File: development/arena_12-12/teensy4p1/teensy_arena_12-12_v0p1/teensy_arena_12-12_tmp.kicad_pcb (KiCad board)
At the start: 4 copper layers, 228.6 x 228.6 mm, 51 parts, among them J1 Barrel_Jack, J2 Conn_01x04, J3 Conn_01x04, P1 CONN15, P10 CONN15, P11 CONN15, P12 CONN15, P2 CONN15, P3 CONN15, P4 CONN15, P5 CONN15, P6 CONN15, P7 CONN15, P8 CONN15, P9 CONN15, Q2 MOSFET_NCHAN, SW1 SW_SPDT, U1 TXB0108PW, U18 Teensy4.1, U2 TXB0108PW, U3 TXB0108PW, U4 TXB0108PW, U5 TXB0108PW

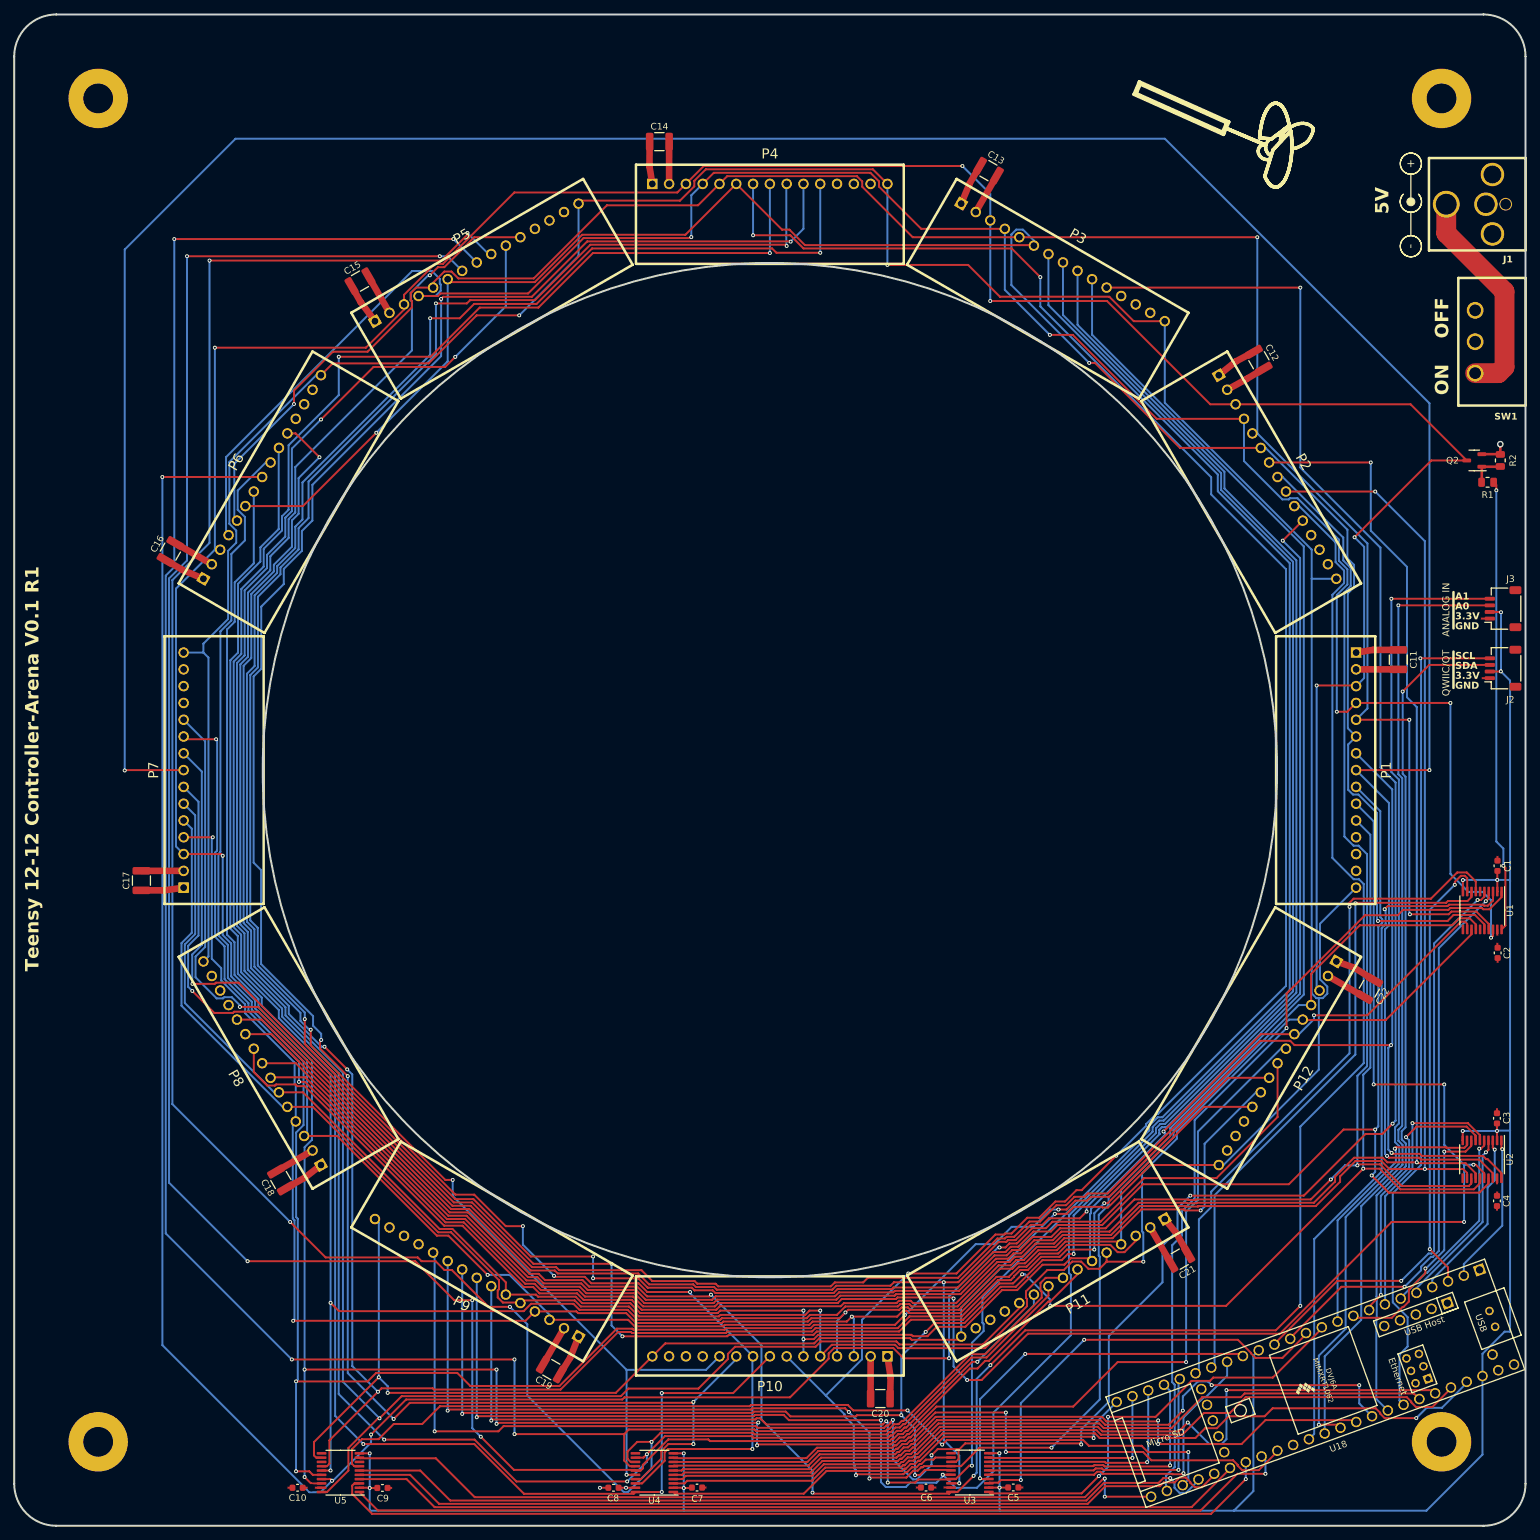
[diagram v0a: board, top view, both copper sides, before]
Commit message: Finished hand route of 12-12 teensy arena. Finished route of 12-12 top.
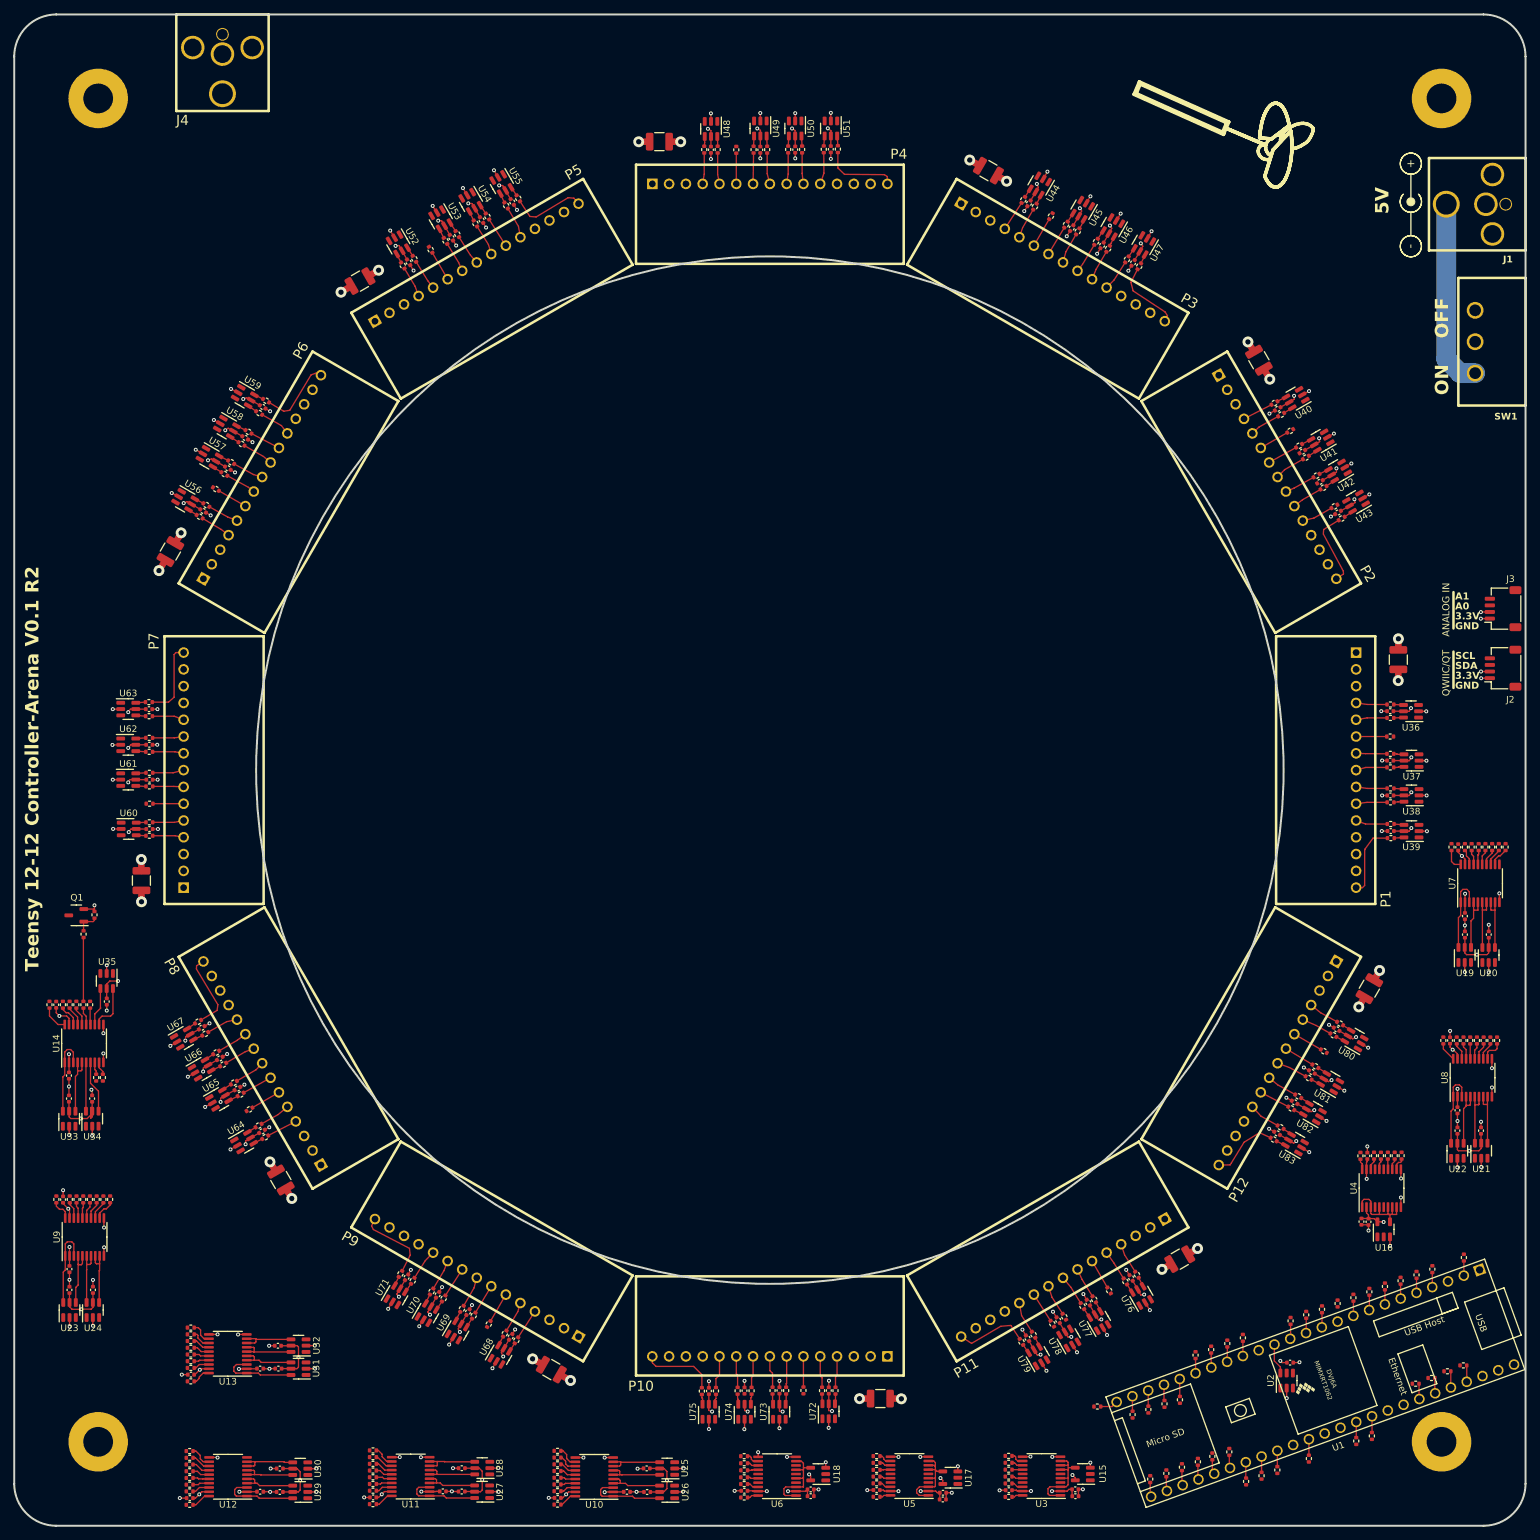
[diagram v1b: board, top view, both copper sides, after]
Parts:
- removed Q2: MOSFET_NCHAN, Package_TO_SOT_SMD:SOT-23-3
- removed the U1 at (285.6, 199.0)
- added C11: 0.1uF, Capacitor_SMD:C_0402_1005Metric, F.Cu at (281.9, 189.5)
- added C12: 0.1uF, Capacitor_SMD:C_0402_1005Metric, F.Cu at (281.8, 229.3)
- added C13: 0.1uF, Capacitor_SMD:C_0402_1005Metric, F.Cu at (280.7, 218.7)
- added C14: 0.1uF, Capacitor_SMD:C_0402_1005Metric, F.Cu at (71.9, 253.3)
- added C15: 0.1uF, Capacitor_SMD:C_0402_1005Metric, F.Cu at (70.9, 242.8)
- added C16: 0.1uF, Capacitor_SMD:C_0402_1005Metric, F.Cu at (156.2, 287.0)
- added C17: 0.1uF, Capacitor_SMD:C_0402_1005Metric, F.Cu at (145.7, 287.9)
- added C18: 0.1uF, Capacitor_SMD:C_0402_1005Metric, F.Cu at (128.3, 286.9)
- added C19: 0.1uF, Capacitor_SMD:C_0402_1005Metric, F.Cu at (117.8, 287.8)
- added C20: 0.1uF, Capacitor_SMD:C_0402_1005Metric, F.Cu at (100.7, 287.0)
- added C21: 0.1uF, Capacitor_SMD:C_0402_1005Metric, F.Cu at (90.1, 287.9)
- added C22: 0.1uF, Capacitor_SMD:C_0402_1005Metric, F.Cu at (100.7, 268.3)
- added C23: 0.1uF, Capacitor_SMD:C_0402_1005Metric, F.Cu at (90.2, 269.2)
- added C24: 0.1uF, Capacitor_SMD:C_0402_1005Metric, F.Cu at (71.8, 224.0)
- added C25: 0.1uF, Capacitor_SMD:C_0402_1005Metric, F.Cu at (69.8, 213.3)
- added C26: 0.1uF, Capacitor_SMD:C_0402_1005Metric, F.Cu at (224.0, 286.6)
- added C27: 0.1uF, Capacitor_SMD:C_0402_1005Metric, F.Cu at (268.4, 246.1)
- added C28: 0.1uF, Capacitor_SMD:C_0402_1005Metric, F.Cu at (204.0, 287.1)
- added C29: 0.1uF, Capacitor_SMD:C_0402_1005Metric, F.Cu at (184.0, 286.6)
- added C30: 0.1uF, Capacitor_SMD:C_0402_1005Metric, F.Cu at (282.9, 202.7)
- added C31: 0.1uF, Capacitor_SMD:C_0402_1005Metric, F.Cu at (286.5, 202.7)
- added C32: 0.1uF, Capacitor_SMD:C_0402_1005Metric, F.Cu at (281.8, 232.3)
- added C33: 0.1uF, Capacitor_SMD:C_0402_1005Metric, F.Cu at (285.4, 232.3)
- added C34: 0.1uF, Capacitor_SMD:C_0402_1005Metric, F.Cu at (71.9, 256.4)
- added C35: 0.1uF, Capacitor_SMD:C_0402_1005Metric, F.Cu at (75.4, 256.4)
- added C36: 0.1uF, Capacitor_SMD:C_0402_1005Metric, F.Cu at (159.2, 283.4)
- added C37: 0.1uF, Capacitor_SMD:C_0402_1005Metric, F.Cu at (159.2, 287.0)
- added C38: 0.1uF, Capacitor_SMD:C_0402_1005Metric, F.Cu at (131.2, 286.9)
- added C39: 0.1uF, Capacitor_SMD:C_0402_1005Metric, F.Cu at (131.2, 283.4)
- added C40: 0.1uF, Capacitor_SMD:C_0402_1005Metric, F.Cu at (103.7, 287.0)
- added C41: 0.1uF, Capacitor_SMD:C_0402_1005Metric, F.Cu at (103.7, 283.4)
- added C42: 0.1uF, Capacitor_SMD:C_0402_1005Metric, F.Cu at (103.5, 268.3)
- added C43: 0.1uF, Capacitor_SMD:C_0402_1005Metric, F.Cu at (103.4, 264.9)
- added C44: 0.1uF, Capacitor_SMD:C_0402_1005Metric, F.Cu at (71.8, 227.5)
- added C45: 0.1uF, Capacitor_SMD:C_0402_1005Metric, F.Cu at (75.3, 227.5)
- added C46: 0.1uF, Capacitor_SMD:C_0402_1005Metric, F.Cu at (77.5, 212.8)
- added C47: 0.1uF, Capacitor_SMD:C_0402_1005Metric, F.Cu at (271.6, 168.9)
- added C48: 0.1uF, Capacitor_SMD:C_0402_1005Metric, F.Cu at (271.6, 176.4)
- added C49: 0.1uF, Capacitor_SMD:C_0402_1005Metric, F.Cu at (271.7, 181.6)
- added C50: 0.1uF, Capacitor_SMD:C_0402_1005Metric, F.Cu at (271.7, 187.0)
- added C51: 0.1uF, Capacitor_SMD:C_0402_1005Metric, F.Cu at (254.6, 123.2)
- added C52: 0.1uF, Capacitor_SMD:C_0402_1005Metric, F.Cu at (258.3, 129.6)
- added C53: 0.1uF, Capacitor_SMD:C_0402_1005Metric, F.Cu at (261.0, 134.2)
- added C54: 0.1uF, Capacitor_SMD:C_0402_1005Metric, F.Cu at (263.7, 138.8)
- added C55: 0.1uF, Capacitor_SMD:C_0402_1005Metric, F.Cu at (217.0, 92.1)
- added C56: 0.1uF, Capacitor_SMD:C_0402_1005Metric, F.Cu at (223.5, 95.8)
- added C57: 0.1uF, Capacitor_SMD:C_0402_1005Metric, F.Cu at (228.1, 98.4)
- added C58: 0.1uF, Capacitor_SMD:C_0402_1005Metric, F.Cu at (232.7, 101.1)
- added C59: 0.1uF, Capacitor_SMD:C_0402_1005Metric, F.Cu at (168.9, 84.0)
- added C60: 0.1uF, Capacitor_SMD:C_0402_1005Metric, F.Cu at (176.4, 84.0)
- added C61: 0.1uF, Capacitor_SMD:C_0402_1005Metric, F.Cu at (181.6, 83.9)
- added C62: 0.1uF, Capacitor_SMD:C_0402_1005Metric, F.Cu at (187.0, 83.9)
- added C63: 0.1uF, Capacitor_SMD:C_0402_1005Metric, F.Cu at (123.2, 101.0)
- added C64: 0.1uF, Capacitor_SMD:C_0402_1005Metric, F.Cu at (129.6, 97.3)
- added C65: 0.1uF, Capacitor_SMD:C_0402_1005Metric, F.Cu at (134.2, 94.6)
- added C66: 0.1uF, Capacitor_SMD:C_0402_1005Metric, F.Cu at (138.8, 91.9)
- added C67: 0.1uF, Capacitor_SMD:C_0402_1005Metric, F.Cu at (92.1, 138.6)
- added C68: 0.1uF, Capacitor_SMD:C_0402_1005Metric, F.Cu at (95.8, 132.1)
- added C69: 0.1uF, Capacitor_SMD:C_0402_1005Metric, F.Cu at (98.4, 127.5)
- added C70: 0.1uF, Capacitor_SMD:C_0402_1005Metric, F.Cu at (101.1, 122.9)
- added C71: 0.1uF, Capacitor_SMD:C_0402_1005Metric, F.Cu at (84.0, 186.7)
- added C72: 0.1uF, Capacitor_SMD:C_0402_1005Metric, F.Cu at (84.0, 179.2)
- added C73: 0.1uF, Capacitor_SMD:C_0402_1005Metric, F.Cu at (83.9, 174.0)
- added C74: 0.1uF, Capacitor_SMD:C_0402_1005Metric, F.Cu at (83.9, 168.6)
- added C75: 0.1uF, Capacitor_SMD:C_0402_1005Metric, F.Cu at (101.0, 232.4)
- added C76: 0.1uF, Capacitor_SMD:C_0402_1005Metric, F.Cu at (97.3, 226.0)
- added C77: 0.1uF, Capacitor_SMD:C_0402_1005Metric, F.Cu at (94.6, 221.4)
- added C78: 0.1uF, Capacitor_SMD:C_0402_1005Metric, F.Cu at (91.9, 216.8)
- added C79: 0.1uF, Capacitor_SMD:C_0402_1005Metric, F.Cu at (138.6, 263.5)
- added C80: 0.1uF, Capacitor_SMD:C_0402_1005Metric, F.Cu at (132.1, 259.8)
- added C81: 0.1uF, Capacitor_SMD:C_0402_1005Metric, F.Cu at (127.5, 257.2)
- added C82: 0.1uF, Capacitor_SMD:C_0402_1005Metric, F.Cu at (122.9, 254.5)
- added C83: 0.1uF, Capacitor_SMD:C_0402_1005Metric, F.Cu at (186.7, 271.6)
- added C84: 0.1uF, Capacitor_SMD:C_0402_1005Metric, F.Cu at (179.2, 271.6)
- added C85: 0.1uF, Capacitor_SMD:C_0402_1005Metric, F.Cu at (174.0, 271.7)
- added C86: 0.1uF, Capacitor_SMD:C_0402_1005Metric, F.Cu at (168.6, 271.7)
- added C87: 0.1uF, Capacitor_SMD:C_0402_1005Metric, F.Cu at (232.4, 254.6)
- added C88: 0.1uF, Capacitor_SMD:C_0402_1005Metric, F.Cu at (226.0, 258.3)
- added C89: 0.1uF, Capacitor_SMD:C_0402_1005Metric, F.Cu at (221.4, 261.0)
- added C90: 0.1uF, Capacitor_SMD:C_0402_1005Metric, F.Cu at (216.8, 263.7)
- added C91: 0.1uF, Capacitor_SMD:C_0402_1005Metric, F.Cu at (263.5, 217.0)
- added C92: 0.1uF, Capacitor_SMD:C_0402_1005Metric, F.Cu at (259.8, 223.5)
- added C93: 0.1uF, Capacitor_SMD:C_0402_1005Metric, F.Cu at (257.2, 228.1)
- added C94: 0.1uF, Capacitor_SMD:C_0402_1005Metric, F.Cu at (254.5, 232.7)
- added J4: Barrel_Jack, arena_custom:DCJACK_2PIN_HIGHCURRENT, F.Cu at (95.0, 63.5)
- added Q1: MOSFET_NCHAN, Package_TO_SOT_SMD:SOT-23-3, F.Cu at (72.9, 199.8)
- added R10: 68, Resistor_SMD:R_0402_1005Metric, F.Cu at (275.6, 254.2)
- added R100: 68, Resistor_SMD:R_0402_1005Metric, F.Cu at (117.8, 282.7)
- added R101: 68, Resistor_SMD:R_0402_1005Metric, F.Cu at (117.8, 281.7)
- added R102: 68, Resistor_SMD:R_0402_1005Metric, F.Cu at (117.8, 280.7)
- added R103: 68, Resistor_SMD:R_0402_1005Metric, F.Cu at (90.0, 288.9)
- added R104: 68, Resistor_SMD:R_0402_1005Metric, F.Cu at (90.0, 286.9)
- added R105: 68, Resistor_SMD:R_0402_1005Metric, F.Cu at (90.0, 285.9)
- added R106: 68, Resistor_SMD:R_0402_1005Metric, F.Cu at (90.0, 284.9)
- added R107: 68, Resistor_SMD:R_0402_1005Metric, F.Cu at (90.0, 283.9)
- added R108: 68, Resistor_SMD:R_0402_1005Metric, F.Cu at (90.0, 282.8)
- added R109: 68, Resistor_SMD:R_0402_1005Metric, F.Cu at (90.0, 281.8)
- added R11: 68, Resistor_SMD:R_0402_1005Metric, F.Cu at (273.2, 255.0)
- added R110: 68, Resistor_SMD:R_0402_1005Metric, F.Cu at (90.0, 280.8)
- added R111: 68, Resistor_SMD:R_0402_1005Metric, F.Cu at (90.2, 270.3)
- added R112: 68, Resistor_SMD:R_0402_1005Metric, F.Cu at (90.2, 268.2)
- added R113: 68, Resistor_SMD:R_0402_1005Metric, F.Cu at (90.2, 267.2)
- added R114: 68, Resistor_SMD:R_0402_1005Metric, F.Cu at (90.2, 266.2)
- added R115: 68, Resistor_SMD:R_0402_1005Metric, F.Cu at (90.2, 265.2)
- added R116: 68, Resistor_SMD:R_0402_1005Metric, F.Cu at (90.2, 264.2)
- added R117: 68, Resistor_SMD:R_0402_1005Metric, F.Cu at (90.2, 263.1)
- added R118: 68, Resistor_SMD:R_0402_1005Metric, F.Cu at (90.2, 262.1)
- added R119: 68, Resistor_SMD:R_0402_1005Metric, F.Cu at (68.8, 213.3)
- added R12: 68, Resistor_SMD:R_0402_1005Metric, F.Cu at (270.8, 255.9)
- added R120: 68, Resistor_SMD:R_0402_1005Metric, F.Cu at (70.9, 213.3)
- added R121: 68, Resistor_SMD:R_0402_1005Metric, F.Cu at (71.9, 213.3)
- added R122: 68, Resistor_SMD:R_0402_1005Metric, F.Cu at (72.9, 213.3)
- added R123: 68, Resistor_SMD:R_0402_1005Metric, F.Cu at (74.0, 213.3)
- added R124: 68, Resistor_SMD:R_0402_1005Metric, F.Cu at (75.0, 213.3)
- added R125: 68, Resistor_SMD:R_0402_1005Metric, F.Cu at (75.9, 224.3)
- added R126: 68, Resistor_SMD:R_0402_1005Metric, F.Cu at (76.9, 224.3)
- added R127: 68, Resistor_SMD:R_0402_1005Metric, F.Cu at (271.7, 167.9)
- added R128: 68, Resistor_SMD:R_0402_1005Metric, F.Cu at (271.7, 169.9)
- added R129: 68, Resistor_SMD:R_0402_1005Metric, F.Cu at (271.7, 175.3)
- added R13: 68, Resistor_SMD:R_0402_1005Metric, F.Cu at (268.5, 256.7)
- added R130: 68, Resistor_SMD:R_0402_1005Metric, F.Cu at (271.7, 177.4)
- added R131: 68, Resistor_SMD:R_0402_1005Metric, F.Cu at (271.7, 180.6)
- added R132: 68, Resistor_SMD:R_0402_1005Metric, F.Cu at (271.7, 182.7)
- added R133: 68, Resistor_SMD:R_0402_1005Metric, F.Cu at (271.7, 186.0)
- added R134: 68, Resistor_SMD:R_0402_1005Metric, F.Cu at (271.7, 188.1)
- added R135: 68, Resistor_SMD:R_0402_1005Metric, F.Cu at (254.1, 122.3)
- added R136: 68, Resistor_SMD:R_0402_1005Metric, F.Cu at (255.1, 124.0)
- added R137: 68, Resistor_SMD:R_0402_1005Metric, F.Cu at (257.8, 128.7)
- added R138: 68, Resistor_SMD:R_0402_1005Metric, F.Cu at (258.9, 130.5)
- added R139: 68, Resistor_SMD:R_0402_1005Metric, F.Cu at (260.5, 133.3)
- added R14: 68, Resistor_SMD:R_0402_1005Metric, F.Cu at (266.1, 257.6)
- added R140: 68, Resistor_SMD:R_0402_1005Metric, F.Cu at (261.5, 135.1)
- added R141: 68, Resistor_SMD:R_0402_1005Metric, F.Cu at (263.2, 137.9)
- added R142: 68, Resistor_SMD:R_0402_1005Metric, F.Cu at (264.3, 139.7)
- added R143: 68, Resistor_SMD:R_0402_1005Metric, F.Cu at (216.1, 91.5)
- added R144: 68, Resistor_SMD:R_0402_1005Metric, F.Cu at (217.9, 92.6)
- added R145: 68, Resistor_SMD:R_0402_1005Metric, F.Cu at (222.6, 95.3)
- added R146: 68, Resistor_SMD:R_0402_1005Metric, F.Cu at (224.4, 96.3)
- added R147: 68, Resistor_SMD:R_0402_1005Metric, F.Cu at (227.1, 97.9)
- added R148: 68, Resistor_SMD:R_0402_1005Metric, F.Cu at (229.0, 98.9)
- added R149: 68, Resistor_SMD:R_0402_1005Metric, F.Cu at (231.8, 100.6)
- added R15: 68, Resistor_SMD:R_0402_1005Metric, F.Cu at (263.7, 258.5)
- added R150: 68, Resistor_SMD:R_0402_1005Metric, F.Cu at (233.7, 101.6)
- added R151: 68, Resistor_SMD:R_0402_1005Metric, F.Cu at (167.9, 83.9)
- added R152: 68, Resistor_SMD:R_0402_1005Metric, F.Cu at (169.9, 83.9)
- added R153: 68, Resistor_SMD:R_0402_1005Metric, F.Cu at (175.3, 83.9)
- added R154: 68, Resistor_SMD:R_0402_1005Metric, F.Cu at (177.4, 83.9)
- added R155: 68, Resistor_SMD:R_0402_1005Metric, F.Cu at (180.6, 83.9)
- added R156: 68, Resistor_SMD:R_0402_1005Metric, F.Cu at (182.7, 83.9)
- added R157: 68, Resistor_SMD:R_0402_1005Metric, F.Cu at (186.0, 83.9)
- added R158: 68, Resistor_SMD:R_0402_1005Metric, F.Cu at (188.1, 83.9)
- added R159: 68, Resistor_SMD:R_0402_1005Metric, F.Cu at (122.3, 101.5)
- added R16: 68, Resistor_SMD:R_0402_1005Metric, F.Cu at (261.3, 259.4)
- added R160: 68, Resistor_SMD:R_0402_1005Metric, F.Cu at (124.0, 100.5)
- added R161: 68, Resistor_SMD:R_0402_1005Metric, F.Cu at (128.7, 97.8)
- added R162: 68, Resistor_SMD:R_0402_1005Metric, F.Cu at (130.5, 96.7)
- added R163: 68, Resistor_SMD:R_0402_1005Metric, F.Cu at (133.3, 95.1)
- added R164: 68, Resistor_SMD:R_0402_1005Metric, F.Cu at (135.1, 94.1)
- added R165: 68, Resistor_SMD:R_0402_1005Metric, F.Cu at (137.9, 92.4)
- added R166: 68, Resistor_SMD:R_0402_1005Metric, F.Cu at (139.7, 91.3)
- added R167: 68, Resistor_SMD:R_0402_1005Metric, F.Cu at (91.5, 139.5)
- added R168: 68, Resistor_SMD:R_0402_1005Metric, F.Cu at (92.6, 137.7)
- added R169: 68, Resistor_SMD:R_0402_1005Metric, F.Cu at (95.3, 133.0)
- added R17: 68, Resistor_SMD:R_0402_1005Metric, F.Cu at (258.9, 260.2)
- added R170: 68, Resistor_SMD:R_0402_1005Metric, F.Cu at (96.3, 131.2)
- added R171: 68, Resistor_SMD:R_0402_1005Metric, F.Cu at (97.9, 128.5)
- added R172: 68, Resistor_SMD:R_0402_1005Metric, F.Cu at (98.9, 126.6)
- added R173: 68, Resistor_SMD:R_0402_1005Metric, F.Cu at (100.6, 123.8)
- added R174: 68, Resistor_SMD:R_0402_1005Metric, F.Cu at (101.6, 121.9)
- added R175: 68, Resistor_SMD:R_0402_1005Metric, F.Cu at (83.9, 187.7)
- added R176: 68, Resistor_SMD:R_0402_1005Metric, F.Cu at (83.9, 185.7)
- added R177: 68, Resistor_SMD:R_0402_1005Metric, F.Cu at (83.9, 180.3)
- added R178: 68, Resistor_SMD:R_0402_1005Metric, F.Cu at (83.9, 178.2)
- added R179: 68, Resistor_SMD:R_0402_1005Metric, F.Cu at (83.9, 175.0)
- added R18: 68, Resistor_SMD:R_0402_1005Metric, F.Cu at (249.4, 263.7)
- added R180: 68, Resistor_SMD:R_0402_1005Metric, F.Cu at (83.9, 172.9)
- added R181: 68, Resistor_SMD:R_0402_1005Metric, F.Cu at (83.9, 169.6)
- added R182: 68, Resistor_SMD:R_0402_1005Metric, F.Cu at (83.9, 167.5)
- added R183: 68, Resistor_SMD:R_0402_1005Metric, F.Cu at (101.5, 233.3)
- added R184: 68, Resistor_SMD:R_0402_1005Metric, F.Cu at (100.5, 231.6)
- added R185: 68, Resistor_SMD:R_0402_1005Metric, F.Cu at (97.8, 226.9)
- added R186: 68, Resistor_SMD:R_0402_1005Metric, F.Cu at (96.7, 225.1)
- added R187: 68, Resistor_SMD:R_0402_1005Metric, F.Cu at (95.1, 222.3)
- added R188: 68, Resistor_SMD:R_0402_1005Metric, F.Cu at (94.1, 220.5)
- added R189: 68, Resistor_SMD:R_0402_1005Metric, F.Cu at (92.4, 217.7)
- added R19: 68, Resistor_SMD:R_0402_1005Metric, F.Cu at (247.0, 264.5)
- added R190: 68, Resistor_SMD:R_0402_1005Metric, F.Cu at (91.3, 215.9)
- added R191: 68, Resistor_SMD:R_0402_1005Metric, F.Cu at (139.5, 264.1)
- added R192: 68, Resistor_SMD:R_0402_1005Metric, F.Cu at (137.7, 263.0)
- added R193: 68, Resistor_SMD:R_0402_1005Metric, F.Cu at (133.0, 260.3)
- added R194: 68, Resistor_SMD:R_0402_1005Metric, F.Cu at (131.2, 259.3)
- added R195: 68, Resistor_SMD:R_0402_1005Metric, F.Cu at (128.5, 257.7)
- added R196: 68, Resistor_SMD:R_0402_1005Metric, F.Cu at (126.6, 256.7)
- added R197: 68, Resistor_SMD:R_0402_1005Metric, F.Cu at (123.8, 255.0)
- added R198: 68, Resistor_SMD:R_0402_1005Metric, F.Cu at (121.9, 254.0)
- added R199: 68, Resistor_SMD:R_0402_1005Metric, F.Cu at (187.7, 271.7)
- added R20: 68, Resistor_SMD:R_0402_1005Metric, F.Cu at (239.8, 273.1)
- added R200: 68, Resistor_SMD:R_0402_1005Metric, F.Cu at (185.7, 271.7)
- added R201: 68, Resistor_SMD:R_0402_1005Metric, F.Cu at (180.3, 271.7)
- added R202: 68, Resistor_SMD:R_0402_1005Metric, F.Cu at (178.2, 271.7)
- added R203: 68, Resistor_SMD:R_0402_1005Metric, F.Cu at (175.0, 271.7)
- added R204: 68, Resistor_SMD:R_0402_1005Metric, F.Cu at (172.9, 271.7)
- added R205: 68, Resistor_SMD:R_0402_1005Metric, F.Cu at (169.6, 271.7)
- added R206: 68, Resistor_SMD:R_0402_1005Metric, F.Cu at (167.5, 271.7)
- added R207: 68, Resistor_SMD:R_0402_1005Metric, F.Cu at (233.3, 254.1)
- added R208: 68, Resistor_SMD:R_0402_1005Metric, F.Cu at (231.6, 255.1)
- added R209: 68, Resistor_SMD:R_0402_1005Metric, F.Cu at (226.9, 257.8)
- added R21: 68, Resistor_SMD:R_0402_1005Metric, F.Cu at (237.5, 273.7)
- added R210: 68, Resistor_SMD:R_0402_1005Metric, F.Cu at (225.1, 258.9)
- added R211: 68, Resistor_SMD:R_0402_1005Metric, F.Cu at (222.3, 260.5)
- added R212: 68, Resistor_SMD:R_0402_1005Metric, F.Cu at (220.5, 261.5)
- added R213: 68, Resistor_SMD:R_0402_1005Metric, F.Cu at (217.7, 263.2)
- added R214: 68, Resistor_SMD:R_0402_1005Metric, F.Cu at (215.9, 264.3)
- added R215: 68, Resistor_SMD:R_0402_1005Metric, F.Cu at (264.1, 216.1)
- added R216: 68, Resistor_SMD:R_0402_1005Metric, F.Cu at (263.0, 217.9)
- added R217: 68, Resistor_SMD:R_0402_1005Metric, F.Cu at (260.3, 222.6)
- added R218: 68, Resistor_SMD:R_0402_1005Metric, F.Cu at (259.3, 224.4)
- added R219: 68, Resistor_SMD:R_0402_1005Metric, F.Cu at (257.7, 227.1)
- added R22: 68, Resistor_SMD:R_0402_1005Metric, F.Cu at (235.1, 274.5)
- added R220: 68, Resistor_SMD:R_0402_1005Metric, F.Cu at (256.7, 229.0)
- added R221: 68, Resistor_SMD:R_0402_1005Metric, F.Cu at (255.0, 231.8)
- added R222: 68, Resistor_SMD:R_0402_1005Metric, F.Cu at (254.0, 233.7)
- added R223: 68, Resistor_SMD:R_0402_1005Metric, F.Cu at (271.6, 172.7)
- added R224: 68, Resistor_SMD:R_0402_1005Metric, F.Cu at (256.5, 126.5)
- added R225: 68, Resistor_SMD:R_0402_1005Metric, F.Cu at (220.3, 94.0)
- added R226: 68, Resistor_SMD:R_0402_1005Metric, F.Cu at (172.7, 84.0)
- added R227: 68, Resistor_SMD:R_0402_1005Metric, F.Cu at (126.5, 99.1)
- added R228: 68, Resistor_SMD:R_0402_1005Metric, F.Cu at (94.0, 135.3)
- added R229: 68, Resistor_SMD:R_0402_1005Metric, F.Cu at (84.0, 182.9)
- added R23: 68, Resistor_SMD:R_0402_1005Metric, F.Cu at (232.7, 275.3)
- added R230: 68, Resistor_SMD:R_0402_1005Metric, F.Cu at (99.1, 229.1)
- added R231: 68, Resistor_SMD:R_0402_1005Metric, F.Cu at (135.3, 261.6)
- added R232: 68, Resistor_SMD:R_0402_1005Metric, F.Cu at (182.9, 271.6)
- added R233: 68, Resistor_SMD:R_0402_1005Metric, F.Cu at (229.1, 256.5)
- added R234: 68, Resistor_SMD:R_0402_1005Metric, F.Cu at (261.6, 220.3)
- added R24: 68, Resistor_SMD:R_0402_1005Metric, F.Cu at (227.3, 274.1)
- added R25: 68, Resistor_SMD:R_0402_1005Metric, F.Cu at (282.7, 267.8)
- added R26: 68, Resistor_SMD:R_0402_1005Metric, F.Cu at (280.3, 268.7)
- added R27: 68, Resistor_SMD:R_0402_1005Metric, F.Cu at (277.9, 269.7)
- added R28: 68, Resistor_SMD:R_0402_1005Metric, F.Cu at (275.5, 270.6)
- added R29: 68, Resistor_SMD:R_0402_1005Metric, F.Cu at (268.9, 278.5)
- added R3: 68, Resistor_SMD:R_0402_1005Metric, F.Cu at (237.8, 284.2)
- added R30: 68, Resistor_SMD:R_0402_1005Metric, F.Cu at (266.5, 279.3)
- added R31: 68, Resistor_SMD:R_0402_1005Metric, F.Cu at (254.6, 283.7)
- added R32: 68, Resistor_SMD:R_0402_1005Metric, F.Cu at (252.2, 284.5)
- added R33: 68, Resistor_SMD:R_0402_1005Metric, F.Cu at (249.8, 285.4)
- added R34: 68, Resistor_SMD:R_0402_1005Metric, F.Cu at (247.3, 280.9)
- added R35: 68, Resistor_SMD:R_0402_1005Metric, F.Cu at (244.7, 281.6)
- added R36: 68, Resistor_SMD:R_0402_1005Metric, F.Cu at (242.5, 282.4)
- added R37: 68, Resistor_SMD:R_0402_1005Metric, F.Cu at (240.1, 283.2)
- added R38: 68, Resistor_SMD:R_0402_1005Metric, F.Cu at (235.3, 285.0)
- added R39: 68, Resistor_SMD:R_0402_1005Metric, F.Cu at (213.9, 287.7)
- added R4: 68, Resistor_SMD:R_0402_1005Metric, F.Cu at (259.3, 281.9)
- added R40: 68, Resistor_SMD:R_0402_1005Metric, F.Cu at (213.9, 285.7)
- added R41: 68, Resistor_SMD:R_0402_1005Metric, F.Cu at (213.9, 284.7)
- added R42: 68, Resistor_SMD:R_0402_1005Metric, F.Cu at (213.9, 283.6)
- added R43: 68, Resistor_SMD:R_0402_1005Metric, F.Cu at (213.9, 282.6)
- added R44: 68, Resistor_SMD:R_0402_1005Metric, F.Cu at (213.9, 281.5)
- added R45: 68, Resistor_SMD:R_0402_1005Metric, F.Cu at (267.1, 236.1)
- added R46: 68, Resistor_SMD:R_0402_1005Metric, F.Cu at (269.2, 236.1)
- added R47: 68, Resistor_SMD:R_0402_1005Metric, F.Cu at (270.2, 236.1)
- added R48: 68, Resistor_SMD:R_0402_1005Metric, F.Cu at (271.3, 236.1)
- added R49: 68, Resistor_SMD:R_0402_1005Metric, F.Cu at (272.3, 236.1)
- added R5: 68, Resistor_SMD:R_0402_1005Metric, F.Cu at (256.6, 261.1)
- added R50: 68, Resistor_SMD:R_0402_1005Metric, F.Cu at (273.4, 236.1)
- added R51: 68, Resistor_SMD:R_0402_1005Metric, F.Cu at (193.9, 287.7)
- added R52: 68, Resistor_SMD:R_0402_1005Metric, F.Cu at (193.9, 285.7)
- added R53: 68, Resistor_SMD:R_0402_1005Metric, F.Cu at (193.9, 284.7)
- added R54: 68, Resistor_SMD:R_0402_1005Metric, F.Cu at (193.9, 283.7)
- added R55: 68, Resistor_SMD:R_0402_1005Metric, F.Cu at (193.9, 282.6)
- added R56: 68, Resistor_SMD:R_0402_1005Metric, F.Cu at (193.9, 281.6)
- added R57: 68, Resistor_SMD:R_0402_1005Metric, F.Cu at (173.9, 287.8)
- added R58: 68, Resistor_SMD:R_0402_1005Metric, F.Cu at (173.9, 285.8)
- added R59: 68, Resistor_SMD:R_0402_1005Metric, F.Cu at (173.9, 284.8)
- added R6: 68, Resistor_SMD:R_0402_1005Metric, F.Cu at (242.2, 266.3)
- added R60: 68, Resistor_SMD:R_0402_1005Metric, F.Cu at (173.9, 283.7)
- added R61: 68, Resistor_SMD:R_0402_1005Metric, F.Cu at (173.9, 282.6)
- added R62: 68, Resistor_SMD:R_0402_1005Metric, F.Cu at (173.9, 281.6)
- added R63: 68, Resistor_SMD:R_0402_1005Metric, F.Cu at (282.9, 189.4)
- added R64: 68, Resistor_SMD:R_0402_1005Metric, F.Cu at (284.0, 189.4)
- added R65: 68, Resistor_SMD:R_0402_1005Metric, F.Cu at (285.0, 189.4)
- added R66: 68, Resistor_SMD:R_0402_1005Metric, F.Cu at (286.0, 189.4)
- added R67: 68, Resistor_SMD:R_0402_1005Metric, F.Cu at (287.1, 189.4)
- added R68: 68, Resistor_SMD:R_0402_1005Metric, F.Cu at (288.1, 189.4)
- added R69: 68, Resistor_SMD:R_0402_1005Metric, F.Cu at (280.9, 189.4)
- added R7: 68, Resistor_SMD:R_0402_1005Metric, F.Cu at (244.6, 265.5)
- added R70: 68, Resistor_SMD:R_0402_1005Metric, F.Cu at (289.1, 189.4)
- added R71: 68, Resistor_SMD:R_0402_1005Metric, F.Cu at (279.7, 218.7)
- added R72: 68, Resistor_SMD:R_0402_1005Metric, F.Cu at (281.7, 218.7)
- added R73: 68, Resistor_SMD:R_0402_1005Metric, F.Cu at (282.7, 218.7)
- added R74: 68, Resistor_SMD:R_0402_1005Metric, F.Cu at (283.7, 218.7)
- added R75: 68, Resistor_SMD:R_0402_1005Metric, F.Cu at (284.7, 218.7)
- added R76: 68, Resistor_SMD:R_0402_1005Metric, F.Cu at (285.8, 218.7)
- added R77: 68, Resistor_SMD:R_0402_1005Metric, F.Cu at (286.8, 218.7)
- added R78: 68, Resistor_SMD:R_0402_1005Metric, F.Cu at (287.8, 218.7)
- added R79: 68, Resistor_SMD:R_0402_1005Metric, F.Cu at (69.9, 242.7)
- added R8: 68, Resistor_SMD:R_0402_1005Metric, F.Cu at (282.8, 251.5)
- added R80: 68, Resistor_SMD:R_0402_1005Metric, F.Cu at (71.9, 242.7)
- added R81: 68, Resistor_SMD:R_0402_1005Metric, F.Cu at (72.9, 242.7)
- added R82: 68, Resistor_SMD:R_0402_1005Metric, F.Cu at (73.9, 242.7)
- added R83: 68, Resistor_SMD:R_0402_1005Metric, F.Cu at (75.0, 242.7)
- added R84: 68, Resistor_SMD:R_0402_1005Metric, F.Cu at (76.0, 242.7)
- added R85: 68, Resistor_SMD:R_0402_1005Metric, F.Cu at (77.0, 242.7)
- added R86: 68, Resistor_SMD:R_0402_1005Metric, F.Cu at (78.0, 242.7)
- added R87: 68, Resistor_SMD:R_0402_1005Metric, F.Cu at (145.7, 288.9)
- added R88: 68, Resistor_SMD:R_0402_1005Metric, F.Cu at (145.7, 286.9)
- added R89: 68, Resistor_SMD:R_0402_1005Metric, F.Cu at (145.7, 285.9)
- added R9: 68, Resistor_SMD:R_0402_1005Metric, F.Cu at (278.0, 253.3)
- added R90: 68, Resistor_SMD:R_0402_1005Metric, F.Cu at (145.7, 284.8)
- added R91: 68, Resistor_SMD:R_0402_1005Metric, F.Cu at (145.7, 283.8)
- added R92: 68, Resistor_SMD:R_0402_1005Metric, F.Cu at (145.7, 282.8)
- added R93: 68, Resistor_SMD:R_0402_1005Metric, F.Cu at (145.7, 281.8)
- added R94: 68, Resistor_SMD:R_0402_1005Metric, F.Cu at (145.7, 280.8)
- added R95: 68, Resistor_SMD:R_0402_1005Metric, F.Cu at (117.8, 288.8)
- added R96: 68, Resistor_SMD:R_0402_1005Metric, F.Cu at (117.8, 286.8)
- added R97: 68, Resistor_SMD:R_0402_1005Metric, F.Cu at (117.8, 285.8)
- added R98: 68, Resistor_SMD:R_0402_1005Metric, F.Cu at (117.8, 284.8)
- added R99: 68, Resistor_SMD:R_0402_1005Metric, F.Cu at (117.8, 283.7)
- added U10: TXB0108PW, Package_SO:TSSOP-20_4.4x6.5mm_P0.65mm, F.Cu at (151.2, 284.7)
- added U11: TXB0108PW, Package_SO:TSSOP-20_4.4x6.5mm_P0.65mm, F.Cu at (123.5, 284.7)
- added U12: TXB0108PW, Package_SO:TSSOP-20_4.4x6.5mm_P0.65mm, F.Cu at (95.8, 284.7)
- added U13: TXB0108PW, Package_SO:TSSOP-20_4.4x6.5mm_P0.65mm, F.Cu at (95.8, 266.1)
- added U14: TXB0108PW, Package_SO:TSSOP-20_4.4x6.5mm_P0.65mm, F.Cu at (74.1, 219.1)
- added U15: 74LVC1G17, Package_TO_SOT_SMD:SOT-23-5, F.Cu at (225.1, 284.3)
- added U16: 74LVC1G17, Package_TO_SOT_SMD:SOT-23-5, F.Cu at (270.6, 247.3)
- added U17: 74LVC1G17, Package_TO_SOT_SMD:SOT-23-5, F.Cu at (205.1, 284.8)
- added U18: 74LVC1G17, Package_TO_SOT_SMD:SOT-23-5, F.Cu at (185.1, 284.3)
- added U19: 74LVC2G17, Package_TO_SOT_SMD:SOT-23-6, F.Cu at (282.9, 205.8)
- added U20: 74LVC2G17, Package_TO_SOT_SMD:SOT-23-6, F.Cu at (286.5, 205.8)
- added U21: 74LVC2G17, Package_TO_SOT_SMD:SOT-23-6, F.Cu at (285.4, 235.4)
- added U22: 74LVC2G17, Package_TO_SOT_SMD:SOT-23-6, F.Cu at (281.8, 235.4)
- added U23: 74LVC2G17, Package_TO_SOT_SMD:SOT-23-6, F.Cu at (71.9, 259.5)
- added U24: 74LVC2G17, Package_TO_SOT_SMD:SOT-23-6, F.Cu at (75.4, 259.5)
- added U25: 74LVC2G17, Package_TO_SOT_SMD:SOT-23-6, F.Cu at (162.3, 283.4)
- added U26: 74LVC2G17, Package_TO_SOT_SMD:SOT-23-6, F.Cu at (162.3, 287.0)
- added U27: 74LVC2G17, Package_TO_SOT_SMD:SOT-23-6, F.Cu at (134.3, 287.0)
- added U28: 74LVC2G17, Package_TO_SOT_SMD:SOT-23-6, F.Cu at (134.3, 283.4)
- added U29: 74LVC2G17, Package_TO_SOT_SMD:SOT-23-6, F.Cu at (106.8, 287.0)
- added U30: 74LVC2G17, Package_TO_SOT_SMD:SOT-23-6, F.Cu at (106.8, 283.5)
- added U31: 74LVC2G17, Package_TO_SOT_SMD:SOT-23-6, F.Cu at (106.5, 268.3)
- added U32: 74LVC2G17, Package_TO_SOT_SMD:SOT-23-6, F.Cu at (106.5, 264.9)
- added U33: 74LVC2G17, Package_TO_SOT_SMD:SOT-23-6, F.Cu at (71.8, 230.5)
- added U34: 74LVC2G17, Package_TO_SOT_SMD:SOT-23-6, F.Cu at (75.3, 230.5)
- added U35: 74LVC2G17, Package_TO_SOT_SMD:SOT-23-6, F.Cu at (77.5, 209.7)
- added U36: 74LVC2G17, Package_TO_SOT_SMD:SOT-23-6, F.Cu at (274.8, 168.9)
- added U37: 74LVC2G17, Package_TO_SOT_SMD:SOT-23-6, F.Cu at (274.9, 176.4)
- added U38: 74LVC2G17, Package_TO_SOT_SMD:SOT-23-6, F.Cu at (274.9, 181.6)
- added U39: 74LVC2G17, Package_TO_SOT_SMD:SOT-23-6, F.Cu at (274.9, 187.0)
- added U40: 74LVC2G17, Package_TO_SOT_SMD:SOT-23-6, F.Cu at (257.3, 121.6)
- added U41: 74LVC2G17, Package_TO_SOT_SMD:SOT-23-6, F.Cu at (261.1, 128.0)
- added U42: 74LVC2G17, Package_TO_SOT_SMD:SOT-23-6, F.Cu at (263.8, 132.6)
- added U43: 74LVC2G17, Package_TO_SOT_SMD:SOT-23-6, F.Cu at (266.5, 137.3)
- added U44: 74LVC2G17, Package_TO_SOT_SMD:SOT-23-6, F.Cu at (218.6, 89.4)
- added U45: 74LVC2G17, Package_TO_SOT_SMD:SOT-23-6, F.Cu at (225.1, 93.0)
- added U46: 74LVC2G17, Package_TO_SOT_SMD:SOT-23-6, F.Cu at (229.6, 95.7)
- added U47: 74LVC2G17, Package_TO_SOT_SMD:SOT-23-6, F.Cu at (234.3, 98.4)
- added U48: 74LVC2G17, Package_TO_SOT_SMD:SOT-23-6, F.Cu at (168.9, 80.8)
- added U49: 74LVC2G17, Package_TO_SOT_SMD:SOT-23-6, F.Cu at (176.4, 80.7)
- added U50: 74LVC2G17, Package_TO_SOT_SMD:SOT-23-6, F.Cu at (181.6, 80.7)
- added U51: 74LVC2G17, Package_TO_SOT_SMD:SOT-23-6, F.Cu at (187.0, 80.7)
- added U52: 74LVC2G17, Package_TO_SOT_SMD:SOT-23-6, F.Cu at (121.6, 98.3)
- added U53: 74LVC2G17, Package_TO_SOT_SMD:SOT-23-6, F.Cu at (128.0, 94.5)
- added U54: 74LVC2G17, Package_TO_SOT_SMD:SOT-23-6, F.Cu at (132.6, 91.8)
- added U55: 74LVC2G17, Package_TO_SOT_SMD:SOT-23-6, F.Cu at (137.3, 89.1)
- added U56: 74LVC2G17, Package_TO_SOT_SMD:SOT-23-6, F.Cu at (89.4, 137.0)
- added U57: 74LVC2G17, Package_TO_SOT_SMD:SOT-23-6, F.Cu at (93.0, 130.5)
- added U58: 74LVC2G17, Package_TO_SOT_SMD:SOT-23-6, F.Cu at (95.7, 126.0)
- added U59: 74LVC2G17, Package_TO_SOT_SMD:SOT-23-6, F.Cu at (98.4, 121.3)
- added U6: TXB0108PW, Package_SO:TSSOP-20_4.4x6.5mm_P0.65mm, F.Cu at (178.9, 284.6)
- added U60: 74LVC2G17, Package_TO_SOT_SMD:SOT-23-6, F.Cu at (80.8, 186.7)
- added U61: 74LVC2G17, Package_TO_SOT_SMD:SOT-23-6, F.Cu at (80.7, 179.2)
- added U62: 74LVC2G17, Package_TO_SOT_SMD:SOT-23-6, F.Cu at (80.7, 174.0)
- added U63: 74LVC2G17, Package_TO_SOT_SMD:SOT-23-6, F.Cu at (80.7, 168.6)
- added U64: 74LVC2G17, Package_TO_SOT_SMD:SOT-23-6, F.Cu at (98.3, 234.0)
- added U65: 74LVC2G17, Package_TO_SOT_SMD:SOT-23-6, F.Cu at (94.5, 227.6)
- added U66: 74LVC2G17, Package_TO_SOT_SMD:SOT-23-6, F.Cu at (91.8, 223.0)
- added U67: 74LVC2G17, Package_TO_SOT_SMD:SOT-23-6, F.Cu at (89.1, 218.3)
- added U68: 74LVC2G17, Package_TO_SOT_SMD:SOT-23-6, F.Cu at (137.0, 266.2)
- added U69: 74LVC2G17, Package_TO_SOT_SMD:SOT-23-6, F.Cu at (130.5, 262.6)
- added U7: TXB0108PW, Package_SO:TSSOP-20_4.4x6.5mm_P0.65mm, F.Cu at (285.2, 194.9)
- added U70: 74LVC2G17, Package_TO_SOT_SMD:SOT-23-6, F.Cu at (126.0, 259.9)
- added U71: 74LVC2G17, Package_TO_SOT_SMD:SOT-23-6, F.Cu at (121.3, 257.2)
- added U72: 74LVC2G17, Package_TO_SOT_SMD:SOT-23-6, F.Cu at (186.7, 274.8)
- added U73: 74LVC2G17, Package_TO_SOT_SMD:SOT-23-6, F.Cu at (179.2, 274.9)
- added U74: 74LVC2G17, Package_TO_SOT_SMD:SOT-23-6, F.Cu at (174.0, 274.9)
- added U75: 74LVC2G17, Package_TO_SOT_SMD:SOT-23-6, F.Cu at (168.6, 274.9)
- added U76: 74LVC2G17, Package_TO_SOT_SMD:SOT-23-6, F.Cu at (234.0, 257.3)
- added U77: 74LVC2G17, Package_TO_SOT_SMD:SOT-23-6, F.Cu at (227.6, 261.1)
- added U78: 74LVC2G17, Package_TO_SOT_SMD:SOT-23-6, F.Cu at (223.0, 263.8)
- added U79: 74LVC2G17, Package_TO_SOT_SMD:SOT-23-6, F.Cu at (218.3, 266.5)
- added U8: TXB0108PW, Package_SO:TSSOP-20_4.4x6.5mm_P0.65mm, F.Cu at (284.1, 224.3)
- added U80: 74LVC2G17, Package_TO_SOT_SMD:SOT-23-6, F.Cu at (266.2, 218.6)
- added U81: 74LVC2G17, Package_TO_SOT_SMD:SOT-23-6, F.Cu at (262.6, 225.1)
- added U82: 74LVC2G17, Package_TO_SOT_SMD:SOT-23-6, F.Cu at (259.9, 229.6)
- added U83: 74LVC2G17, Package_TO_SOT_SMD:SOT-23-6, F.Cu at (257.2, 234.3)
- added U9: TXB0108PW, Package_SO:TSSOP-20_4.4x6.5mm_P0.65mm, F.Cu at (74.1, 248.4)
- C1, C10, C2, C3, C4, C5, C6, C7, C8, C9: footprint Capacitor_SMD:C_0603_1608Metric -> Capacitor_SMD:C_0402_1005Metric
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- renumbered C16 to C100, C17 to C101, C18 to C102, C19 to C103, C20 to C104, C21 to C105, C22 to C106, C11 to C95, C12 to C96, C13 to C97, C14 to C98, C15 to C99
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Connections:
- net /Panel Headers/RESET renamed /Panel Headers/HDR_RESET
- C10 pad 1: +5V -> +3.3V
- C2 pad 1: +5V -> +3.3V
- C3 pad 1: +3.3V -> +5V
- C4 pad 1: +5V -> +3.3V
- C5 pad 1: +3.3V -> +5V
- C6 pad 1: +5V -> +3.3V
- C7 pad 1: +3.3V -> +5V
- C8 pad 1: +5V -> +3.3V
- C9 pad 1: +3.3V -> +5V
- P1 pad 10: /Level Shifters/PAN5V.CS_03 -> /Panel Headers/HDR_CS_03_P1
- P1 pad 11: /Level Shifters/PAN5V.CS_04 -> /Panel Headers/HDR_CS_04_P1
- P1 pad 15: /Level Shifters/PAN5V.EXT_INT -> /Panel Headers/HDR_EXT_INT_P1
- P1 pad 4: /Level Shifters/PAN5V.SCK_0 -> /Panel Headers/HDR_SCK_0_P1
- P1 pad 5: /Level Shifters/PAN5V.MOSI_0 -> /Panel Headers/HDR_MOSI_0_P1
- P1 pad 6: /Level Shifters/PAN5V.MISO_0 -> /Panel Headers/HDR_MISO_0_P1
- P1 pad 7: /Level Shifters/PAN5V.CS_00 -> /Panel Headers/HDR_CS_00_P1
- P1 pad 8: /Level Shifters/PAN5V.CS_01 -> /Panel Headers/HDR_CS_01_P1
- P1 pad 9: /Level Shifters/PAN5V.CS_02 -> /Panel Headers/HDR_CS_02_P1
- P10 pad 10: /Level Shifters/PAN5V.CS_18 -> /Panel Headers/HDR_CS_18_P10
- P10 pad 11: /Level Shifters/PAN5V.CS_19 -> /Panel Headers/HDR_CS_19_P10
- P10 pad 15: /Level Shifters/PAN5V.EXT_INT -> /Panel Headers/HDR_EXT_INT_P10
- P10 pad 4: /Level Shifters/PAN5V.SCK_1 -> /Panel Headers/HDR_SCK_1_P10
- P10 pad 5: /Level Shifters/PAN5V.MOSI_1 -> /Panel Headers/HDR_MOSI_1_P10
- P10 pad 6: /Level Shifters/PAN5V.MISO_1 -> /Panel Headers/HDR_MISO_1_P10
- P10 pad 7: /Level Shifters/PAN5V.CS_15 -> /Panel Headers/HDR_CS_15_P10
- P10 pad 8: /Level Shifters/PAN5V.CS_16 -> /Panel Headers/HDR_CS_16_P10
- P10 pad 9: /Level Shifters/PAN5V.CS_17 -> /Panel Headers/HDR_CS_17_P10
- P11 pad 10: /Level Shifters/PAN5V.CS_23 -> /Panel Headers/HDR_CS_23_P11
- P11 pad 11: /Level Shifters/PAN5V.CS_24 -> /Panel Headers/HDR_CS_24_P11
- P11 pad 15: /Level Shifters/PAN5V.EXT_INT -> /Panel Headers/HDR_EXT_INT_P11
- P11 pad 4: /Level Shifters/PAN5V.SCK_1 -> /Panel Headers/HDR_SCK_1_P11
- P11 pad 5: /Level Shifters/PAN5V.MOSI_1 -> /Panel Headers/HDR_MOSI_1_P11
- P11 pad 6: /Level Shifters/PAN5V.MISO_1 -> /Panel Headers/HDR_MISO_1_P11
- P11 pad 7: /Level Shifters/PAN5V.CS_20 -> /Panel Headers/HDR_CS_20_P11
- P11 pad 8: /Level Shifters/PAN5V.CS_21 -> /Panel Headers/HDR_CS_21_P11
- P11 pad 9: /Level Shifters/PAN5V.CS_22 -> /Panel Headers/HDR_CS_22_P11
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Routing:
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- added copper zone on In2.Cu, net +3.3V
- added copper zone on In3.Cu, net +3.3V
- added copper zone on In4.Cu, net GND
- removed copper zone on In2.Cu, net +5V
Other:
- outline, holes or cut-outs redrawn
- copper layers 4 -> 6
- board text added: "Teensy 12-12 Controller-Arena V0.1 R2"
- board text removed: "Teensy 12-12 Controller-Arena V0.1 R1"
